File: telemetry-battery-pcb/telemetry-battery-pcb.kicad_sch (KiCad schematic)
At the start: 71 parts, among them J1 Network Connector, J3 CONN_360410_MZC, J4 DS18B20, J5 CONN_360410_MZC, Q1 NMOS, Q2 PMOS, Q4 NMOS, U4 LTC2944, U5 XR76208, U6 M24C02-WMN, U7 Tps1htc, U8 DS2484R

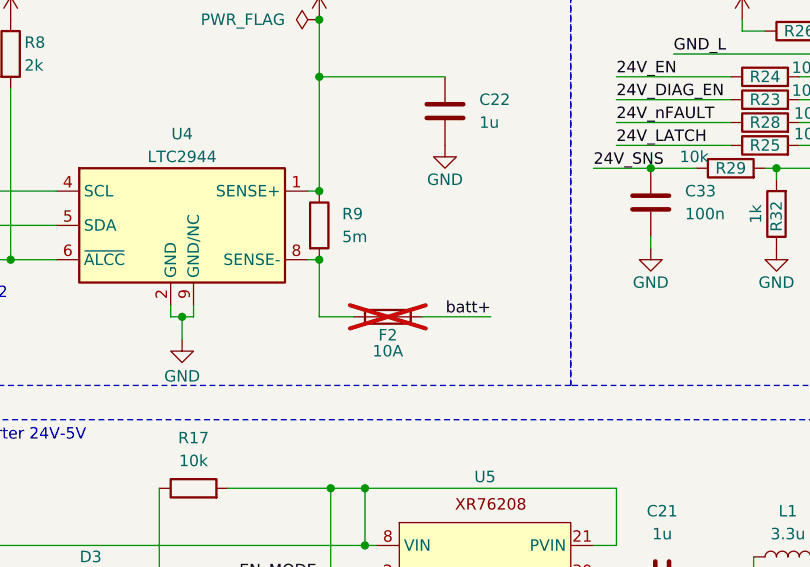
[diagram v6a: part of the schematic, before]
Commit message: telemetry-battery-pcb: add fixes for template
- Added an extra footprint for a fuse
- Increased LED resistor value
- Rounded board corners
- Changed temperature sensor connector for horizontal version (not from
  template)
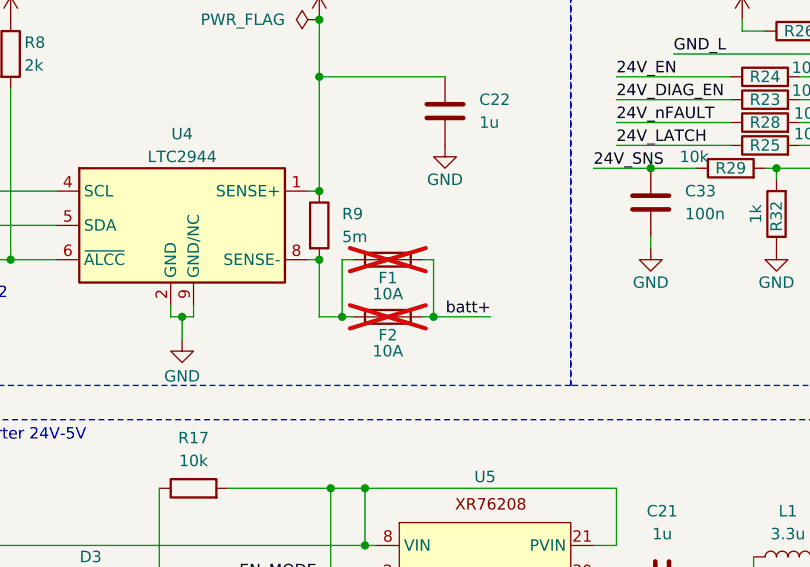
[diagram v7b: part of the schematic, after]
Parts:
- added F1: 10A, Fuse:Fuseholder_Clip-5x20mm_Littelfuse_111_Lateral_P18.80x5.00mm_D1.17mm_Horizontal, symbol Device:Fuse
- J4: footprint Connector_JST:JST_PH_B3B-PH-K_1x03_P2.00mm_Vertical -> Connector_JST:JST_PH_S3B-PH-K_1x03_P2.00mm_Horizontal; JLCPCB C131339 -> (none)
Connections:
- net batt+: now also F1.2
- net at F2.1, R9.2, U4.8 (SENSE-): now also F1.1
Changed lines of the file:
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@@
 	)
 	(junction
+		(at 81.28 88.9)
+		(diameter 0)
+		(color 0 0 0 0)
+	)
+	(junction
 		(at 142.24 115.57)
 		(diameter 0)
@@
 	)
 	(junction
+		(at 71.12 88.9)
+		(diameter 0)
+		(color 0 0 0 0)
+	)
+	(junction
 		(at 34.29 82.55)
 		(diameter 0)
@@
 	(wire
 		(pts
+			(xy 80.01 82.55) (xy 81.28 82.55)
+		)
+		(stroke
+			(width 0)
+			(type default)
+		)
+	)
+	(wire
+		(pts
 			(xy 25.4 171.45) (xy 25.4 173.99)
 		)
@@
 		)
 	)
+	(wire
+		(pts
+			(xy 72.39 82.55) (xy 71.12 82.55)
+		)
+		(stroke
+			(width 0)
+			(type default)
+		)
+	)
 	(polyline
 		(pts
@@
 	(wire
 		(pts
+			(xy 81.28 88.9) (xy 80.01 88.9)
+		)
+		(stroke
+			(width 0)
+			(type default)
+		)
+	)
+	(wire
+		(pts
 			(xy 163.83 132.08) (xy 185.42 132.08)
 		)
@@
 	(wire
 		(pts
+			(xy 71.12 88.9) (xy 72.39 88.9)
+		)
+		(stroke
+			(width 0)
+			(type default)
+		)
+	)
+	(wire
+		(pts
 			(xy 125.73 115.57) (xy 125.73 116.84)
 		)
@@
 	(wire
 		(pts
+			(xy 81.28 82.55) (xy 81.28 88.9)
+		)
+		(stroke
+			(width 0)
+			(type default)
+		)
+	)
+	(wire
+		(pts
 			(xy 154.94 69.85) (xy 154.94 72.39)
 		)
@@
 	(wire
 		(pts
+			(xy 71.12 82.55) (xy 71.12 88.9)
+		)
+		(stroke
+			(width 0)
+			(type default)
+		)
+	)
+	(wire
+		(pts
 			(xy 21.59 124.46) (xy 21.59 125.73)
 		)
@@
 	(wire
 		(pts
-			(xy 68.58 88.9) (xy 72.39 88.9)
+			(xy 68.58 88.9) (xy 71.12 88.9)
 		)
 		(stroke
@@
 	(wire
 		(pts
-			(xy 87.63 88.9) (xy 80.01 88.9)
+			(xy 87.63 88.9) (xy 81.28 88.9)
 		)
 		(stroke
@@
 	)
 	(symbol
+		(lib_id "Device:Fuse")
+		(at 76.2 82.55 90)
+		(unit 1)
+		(exclude_from_sim no)
+		(in_bom yes)
+		(on_board yes)
+		(dnp yes)
+		(property "Reference" "F1"
+			(at 76.2 84.582 90)
+			(effects
+				(font
+					(size 1.27 1.27)
+				)
+			)
+		)
+		(property "Value" "10A"
+			(at 76.2 86.36 90)
+			(effects
+				(font
+					(size 1.27 1.27)
+				)
+			)
+		)
+		(property "Footprint" "Fuse:Fuseholder_Clip-5x20mm_Littelfuse_111_Lateral_P18.80x5.00mm_D1.17mm_Horizontal"
+			(at 76.2 84.328 90)
+			(effects
+				(font
+					(size 1.27 1.27)
+				)
+				(hide yes)
+			)
+		)
+		(property "Datasheet" "~"
+			(at 76.2 82.55 0)
+			(effects
+				(font
+					(size 1.27 1.27)
+				)
+				(hide yes)
+			)
+		)
+		(property "Description" "Fuse"
+			(at 76.2 82.55 0)
+			(effects
+				(font
+					(size 1.27 1.27)
+				)
+				(hide yes)
+			)
+		)
+		(pin "1"
+		)
+		(pin "2"
+		)
+		(instances
+			(project "telemetry-battery-pcb"
+				(path "/4b4cf3aa-c94c-4150-b9c5-35049cd71136"
+					(reference "F1")
+					(unit 1)
+				)
+			)
+		)
+	)
+	(symbol
 		(lib_id "Device:D_Zener")
 		(at 43.18 118.11 180)
@@
 			)
 		)
-		(property "Footprint" "Connector_JST:JST_PH_B3B-PH-K_1x03_P2.00mm_Vertical"
+		(property "Footprint" "Connector_JST:JST_PH_S3B-PH-K_1x03_P2.00mm_Horizontal"
 			(at 260.35 139.7 0)
 			(effects
@@
 			(at 260.35 139.7 0)
 			(effects
-				(font
-					(size 1.27 1.27)
-				)
-				(hide yes)
-			)
-		)
-		(property "JLCPCB" "C131339"
-			(at 260.35 139.7 0)
-			(effects

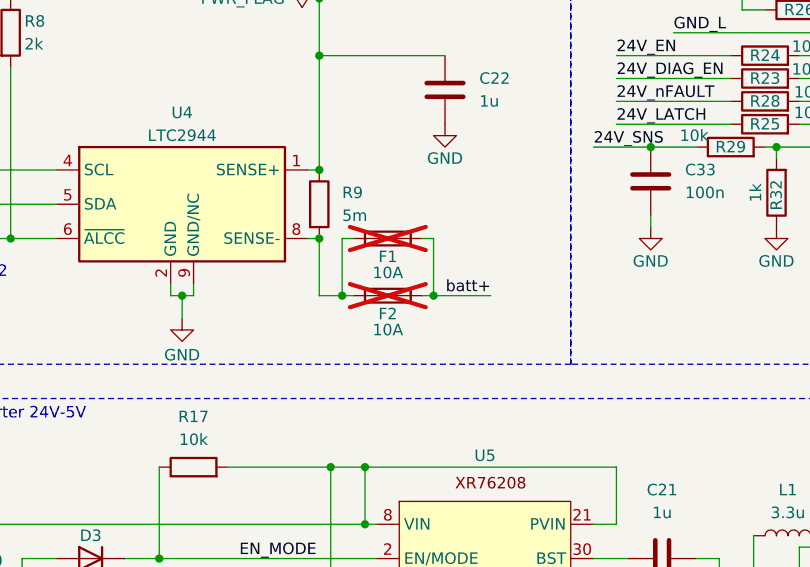
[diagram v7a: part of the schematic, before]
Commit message: telemetry-battery-pcb: add combined fuseholder footprint
This gets rid of all remaining DRC warnings and makes the schematic a
little clearer.
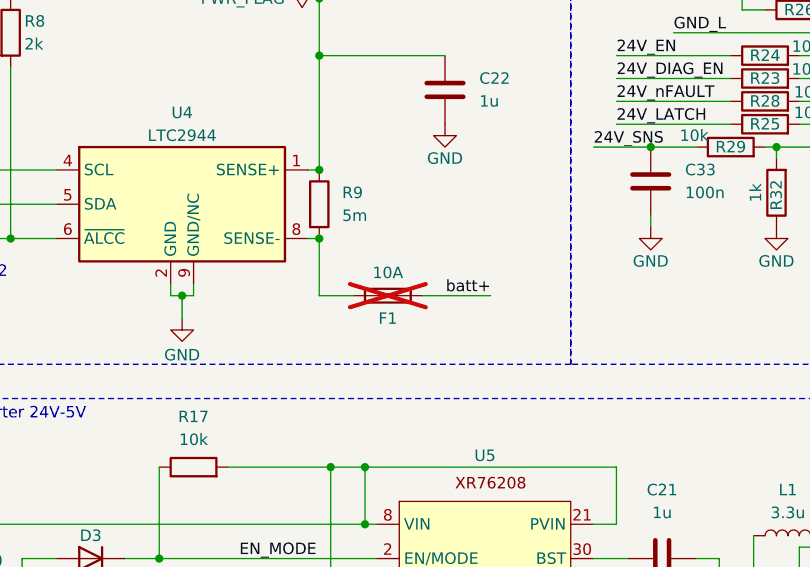
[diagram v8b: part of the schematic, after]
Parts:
- removed F2: 10A, Exocet:Fuse_Holder_Littelfuse_01530008, symbol Device:Fuse
- F1: footprint Fuse:Fuseholder_Clip-5x20mm_Littelfuse_111_Lateral_P18.80x5.00mm_D1.17mm_Horizontal -> Exocet:Fuseholder_Littelfuse_Combined
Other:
- moved on the sheet: F1
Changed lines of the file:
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@@
 	)
 	(junction
-		(at 81.28 88.9)
-		(diameter 0)
-		(color 0 0 0 0)
-	)
-	(junction
 		(at 142.24 115.57)
 		(diameter 0)
@@
 	)
 	(junction
-		(at 71.12 88.9)
-		(diameter 0)
-		(color 0 0 0 0)
-	)
-	(junction
 		(at 34.29 82.55)
 		(diameter 0)
@@
 	(wire
 		(pts
-			(xy 80.01 82.55) (xy 81.28 82.55)
+			(xy 80.01 88.9) (xy 87.63 88.9)
 		)
 		(stroke
@@
 		)
 	)
-	(wire
-		(pts
-			(xy 72.39 82.55) (xy 71.12 82.55)
-		)
-		(stroke
-			(width 0)
-			(type default)
-		)
-	)
 	(polyline
 		(pts
@@
 	(wire
 		(pts
-			(xy 81.28 88.9) (xy 80.01 88.9)
-		)
-		(stroke
-			(width 0)
-			(type default)
-		)
-	)
-	(wire
-		(pts
 			(xy 163.83 132.08) (xy 185.42 132.08)
 		)
@@
 	(wire
 		(pts
-			(xy 71.12 88.9) (xy 72.39 88.9)
-		)
-		(stroke
-			(width 0)
-			(type default)
-		)
-	)
-	(wire
-		(pts
 			(xy 125.73 115.57) (xy 125.73 116.84)
 		)
@@
 	(wire
 		(pts
-			(xy 81.28 82.55) (xy 81.28 88.9)
-		)
-		(stroke
-			(width 0)
-			(type default)
-		)
-	)
-	(wire
-		(pts
 			(xy 154.94 69.85) (xy 154.94 72.39)
 		)
@@
 	(wire
 		(pts
-			(xy 71.12 82.55) (xy 71.12 88.9)
-		)
-		(stroke
-			(width 0)
-			(type default)
-		)
-	)
-	(wire
-		(pts
 			(xy 21.59 124.46) (xy 21.59 125.73)
 		)
@@
 	(wire
 		(pts
-			(xy 68.58 88.9) (xy 71.12 88.9)
+			(xy 68.58 88.9) (xy 72.39 88.9)
 		)
 		(stroke
@@
 	(wire
 		(pts
-			(xy 87.63 88.9) (xy 81.28 88.9)
-		)
-		(stroke
-			(width 0)
-			(type default)
-		)
-	)
-	(wire
-		(pts
 			(xy 25.4 78.74) (xy 39.37 78.74)
 		)
@@
 	(symbol
 		(lib_id "Device:Fuse")
-		(at 76.2 82.55 90)
+		(at 76.2 88.9 90)
 		(unit 1)
 		(exclude_from_sim no)
@@
 		(dnp yes)
 		(property "Reference" "F1"
-			(at 76.2 84.582 90)
+			(at 76.2 91.44 90)
 			(effects
 				(font
@@
 			)
 		)
-		(property "Footprint" "Fuse:Fuseholder_Clip-5x20mm_Littelfuse_111_Lateral_P18.80x5.00mm_D1.17mm_Horizontal"
-			(at 76.2 84.328 90)
+		(property "Footprint" "Exocet:Fuseholder_Littelfuse_Combined"
+			(at 76.2 90.678 90)
 			(effects
 				(font
@@
 		)
 		(property "Datasheet" "~"
-			(at 76.2 82.55 0)
+			(at 76.2 88.9 0)
 			(effects
 				(font
@@
 			)
 		)
-		(property "Description" "Fuse"
-			(at 76.2 82.55 0)
+		(property "Description" ""
+			(at 76.2 86.36 90)
 			(effects
 				(font
@@
 					(unit 1)
 				)
-			)
-		)
-	)
-	(symbol
-		(lib_id "Device:Fuse")
-		(at 76.2 88.9 90)
-		(unit 1)
-		(exclude_from_sim no)
-		(in_bom yes)
-		(on_board yes)
-		(dnp yes)
-		(property "Reference" "F2"
-			(at 76.2 90.932 90)
-			(effects
-				(font
-					(size 1.27 1.27)
-				)
-			)
-		)
-		(property "Value" "10A"
-			(at 76.2 92.71 90)
-			(effects
-				(font
-					(size 1.27 1.27)
-				)
-			)
-		)
-		(property "Footprint" "Exocet:Fuse_Holder_Littelfuse_01530008"
-			(at 76.2 90.678 90)
-			(effects
-				(font
-					(size 1.27 1.27)
-				)
-				(hide yes)
-			)
-		)
-		(property "Datasheet" "~"
-			(at 76.2 88.9 0)
-			(effects
-				(font
-					(size 1.27 1.27)
-				)
-				(hide yes)
-			)
-		)
-		(property "Description" "Fuse"
-			(at 76.2 88.9 0)
-			(effects
-				(font
-					(size 1.27 1.27)
-				)
-				(hide yes)
-			)
-		)
-		(property "JLCPCB" "C206907"
-			(at 76.2 88.9 0)
-			(effects
-				(font
-					(size 1.27 1.27)
-				)
-				(hide yes)
-			)
-		)
-		(pin "1"
-		)
-		(pin "2"
-		)
-		(instances
-			(project "telemetry-battery-pcb"
-				(path "/4b4cf3aa-c94c-4150-b9c5-35049cd71136"
-					(reference "F2")
-					(unit 1)
-				)
